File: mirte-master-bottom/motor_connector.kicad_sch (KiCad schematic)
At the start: 11 parts, among them J7 Motor_conn, Q5 SiA483DJ, U3 DRV8231DDAR

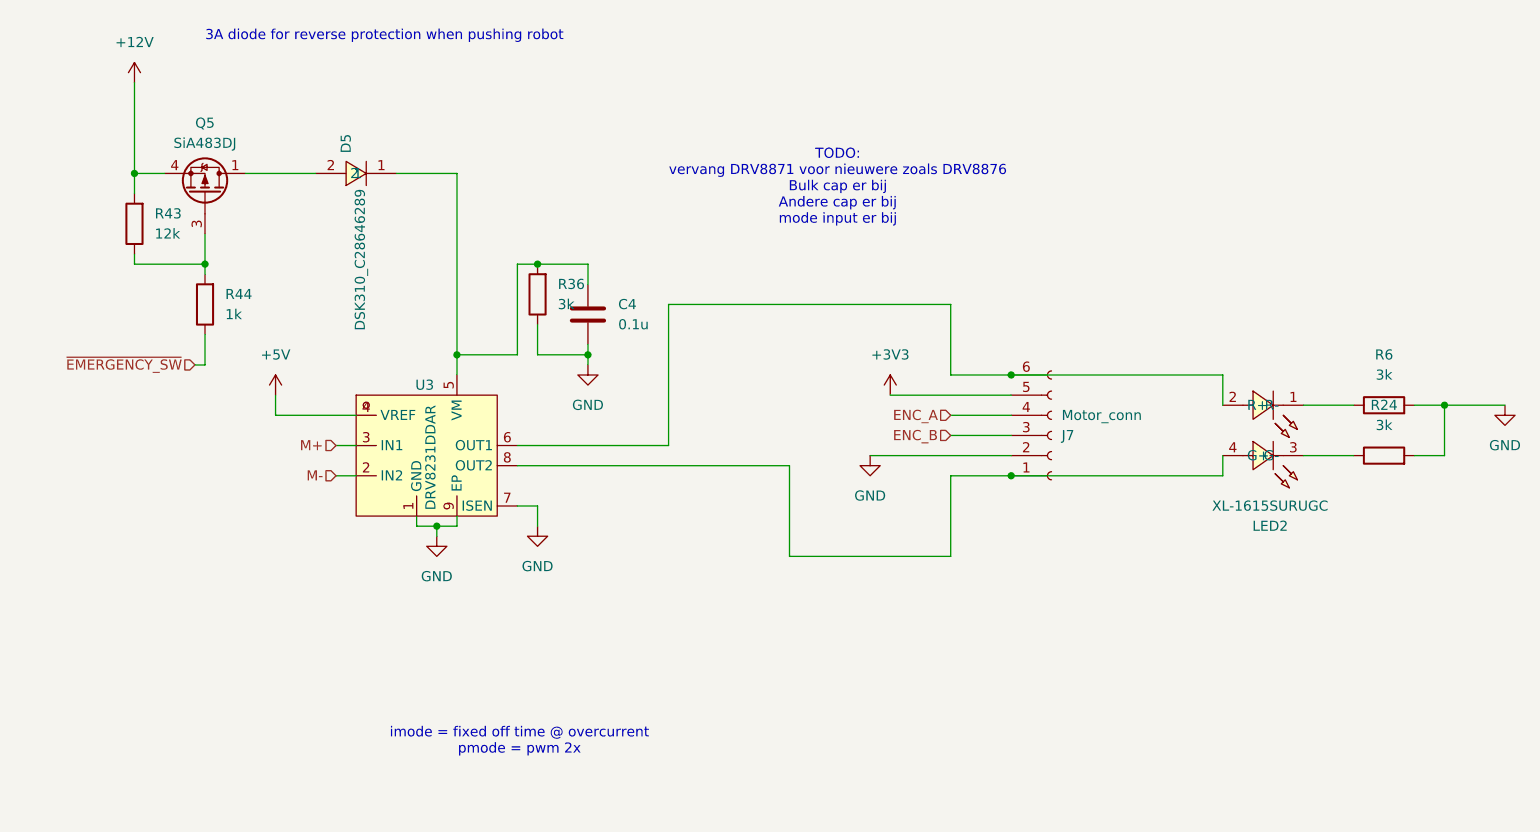
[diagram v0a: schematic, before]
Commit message: MM: Fix diode blowing up drv
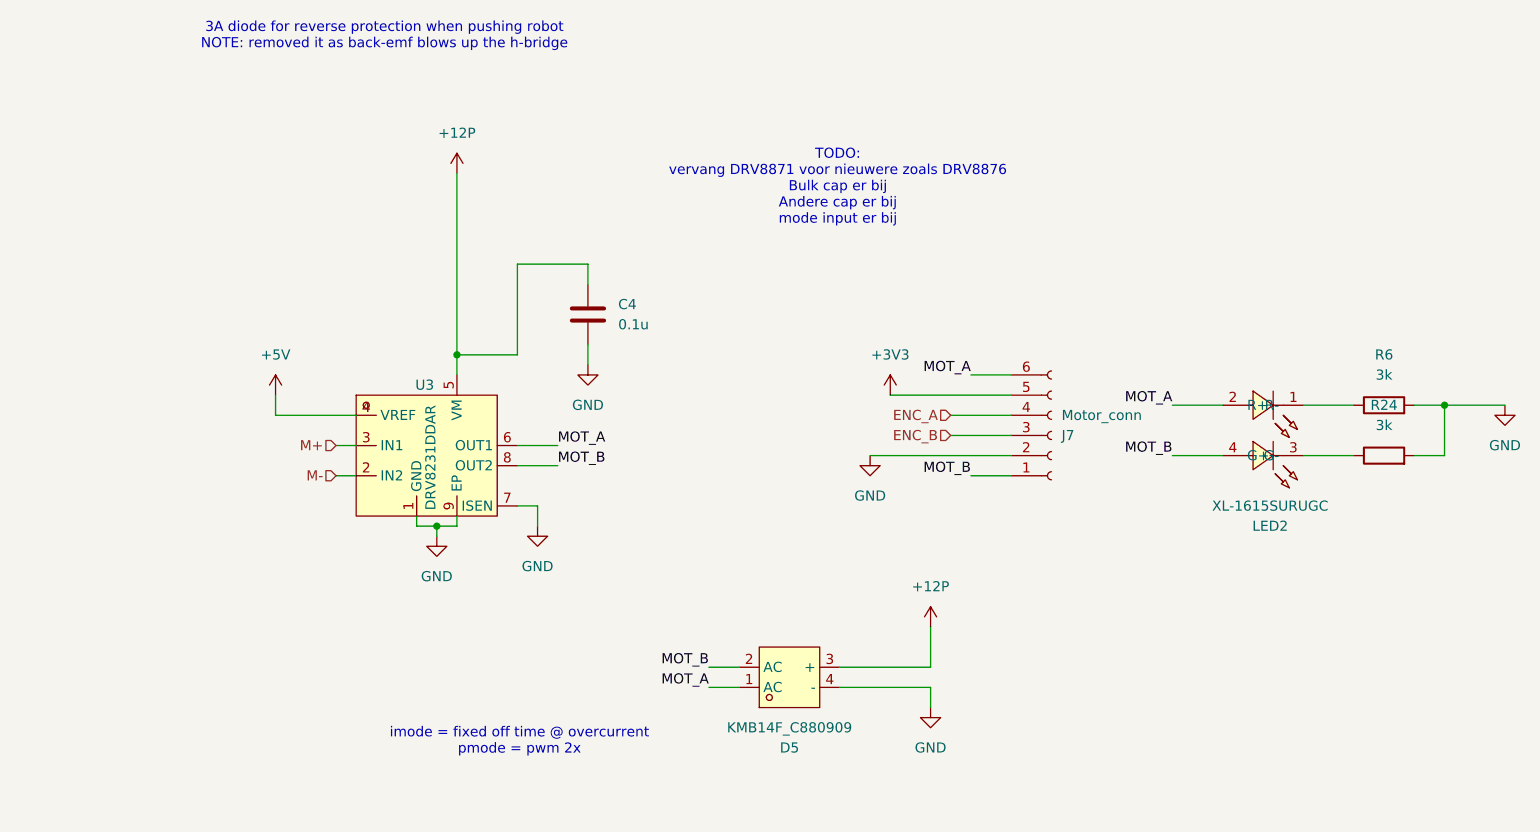
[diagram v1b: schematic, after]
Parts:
- removed D5: DSK310_C28646289, easyeda:SOD-123FL_L2.8-W1.9-LS3.7-RD, symbol easyeda:DSK310_C28646289
- removed Q5: SiA483DJ, Package_TO_SOT_SMD:Vishay_PowerPAK_SC70-6L_Single, symbol Transistor_FET:SiA449DJ
- removed R36: 3k, Resistor_SMD:R_0805_2012Metric, symbol Device:R
- removed R43: 12k, Resistor_SMD:R_0805_2012Metric, symbol Device:R
- removed R44: 1k, Resistor_SMD:R_0805_2012Metric, symbol Device:R
- added D5: KMB14F_C880909, easyeda:MBF-SMD_L4.8-W3.8-P2.54-LS6.8-TL, symbol easyeda:KMB14F_C880909
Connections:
- net GND: now also D5.4 (-)
- net +12P: now reaches C4.1, U3.5 (VM)
- net +12P: now also D5.3 (+)
- net MOT_A: now reaches J7.6 (Pin_6), LED2.2 (R+), U3.6 (OUT1)
- net MOT_A: now also D5.1 (AC)
- net MOT_B: now reaches J7.1 (Pin_1), LED2.4 (G+), U3.8 (OUT2)
- net MOT_B: now also D5.2 (AC)
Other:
- note added: "3A diode for reverse protection when pushing robot NOTE: removed it as back-emf blows up the h-bridge"
- note removed: "3A diode for reverse protection when pushing robot"

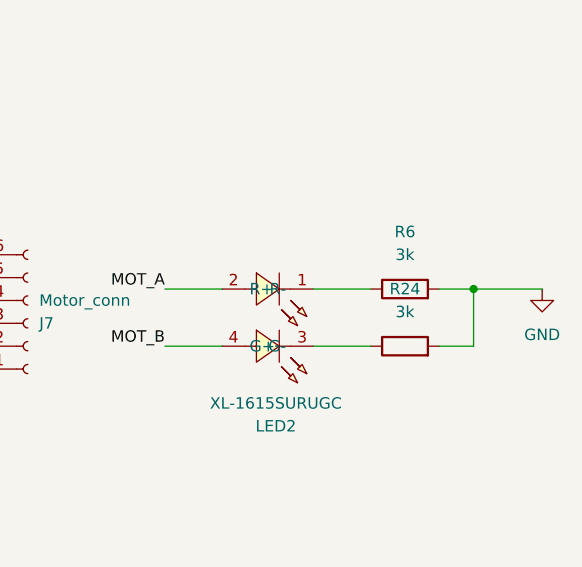
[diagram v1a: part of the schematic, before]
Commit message: MM: Leds less bright, reorder oled/sonar conns, move parts
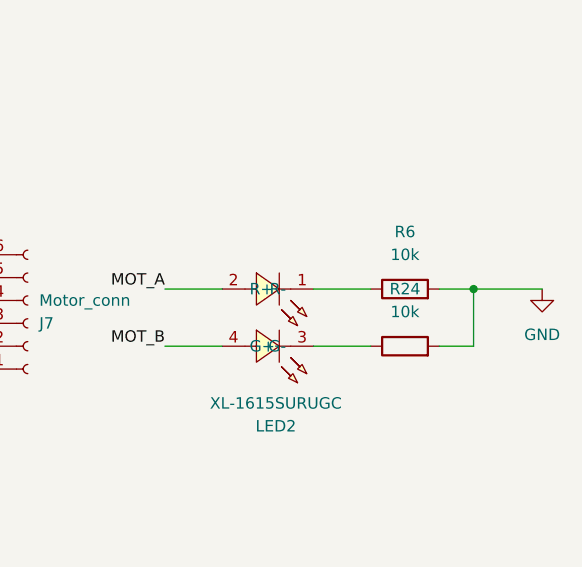
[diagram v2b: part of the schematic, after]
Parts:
- C4: LCSC (none) -> C49678
- D5: LCSC (none) -> C880909
- J7: LCSC (none) -> C131342
- LED2: LCSC (none) -> C965839
- R24, R6: value 3k -> 10k; LCSC (none) -> C17414
- U3: LCSC (none) -> C5218850
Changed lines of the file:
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@@
+			)
+		)
+		(property "LCSC" "C5218850"
+			(at 58.166 69.85 0)
+			(effects
+				(font
+					(size 1.27 1.27)
+				)
+				(hide yes)
 			)
 		)
@@
 			)
 		)
-		(property "Value" "3k"
+		(property "Value" "10k"
 			(at 179.07 68.58 90)
 			(effects
@@
 		(property "Description" "Resistor"
 			(at 179.07 72.39 0)
+			(effects
+				(font
+					(size 1.27 1.27)
+				)
+				(hide yes)
+			)
+		)
+		(property "LCSC" "C17414"
+			(at 179.07 66.04 0)
 			(effects
 				(font
@@
 			)
 		)
-		(property "Value" "3k"
+		(property "Value" "10k"
 			(at 179.07 74.93 90)
 			(effects
@@
 		(property "Description" "Resistor"
 			(at 179.07 78.74 0)
+			(effects
+				(font
+					(size 1.27 1.27)
+				)
+				(hide yes)
+			)
+		)
+		(property "LCSC" "C17414"
+			(at 179.07 72.39 0)
 			(effects
 				(font
@@
 			)
 		)
+		(property "LCSC" "C131342"
+			(at 138.43 76.2 0)
+			(effects
+				(font
+					(size 1.27 1.27)
+				)
+				(hide yes)
+			)
+		)
 		(pin "5"
 		)
@@
 			)
 		)
+		(property "LCSC" "C49678"
+			(at 82.55 59.6899 0)
+			(effects
+				(font
+					(size 1.27 1.27)
+				)
+				(hide yes)
+			)
+		)
 		(pin "1"
 		)
@@
 			)
 		)
+		(property "LCSC" "C965839"
+			(at 164.72 87.63 0)
+			(effects
+				(font
+					(size 1.27 1.27)
+				)
+				(hide yes)
+			)
+		)
 		(pin "4"
 		)
@@
 			(effects
 				(font
+					(size 1.27 1.27)
+				)
+				(hide yes)
+			)
+		)
+		(property "LCSC" "C880909"
+			(at 104.14 115.57 0)
+			(effects
+				(font

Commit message: MM: Add R_trip & bulk cap drv8870
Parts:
- added C18: 47uF, easyeda:CAP-SMD_BD6.3-L6.6-W6.6-LS7.6-FD, symbol easyeda:RVT1H470M0607
- added R36: 0.2, Resistor_SMD:R_0805_2012Metric, symbol Device:R
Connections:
- net +12P: now also C18.1
- net +3V3: now also U3.4 (VREF)
- net +5V: no longer U3.4 (VREF)
- net GND: now also C18.2, R36.1; no longer U3.7 (ISEN)
- new net: R36.2, U3.7 (ISEN)
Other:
- note added: "I_{trip} = V_{ref}/(10*R_{sen}) 1.5 = 5/4 Rsense use: I_{rms}^{2} * R = 0.5^2 * 3 = 0.75W 3v3: 1.5 = 3.3/(10*0.2) 0.5^2*0.2 = 0.05W USE 3v3!!!"
- note removed: "imode = fixed off time @ overcurrent pmode = pwm 2x"
